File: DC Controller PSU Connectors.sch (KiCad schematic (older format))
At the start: 9 parts, among them J1 SM08B-CPTK-1A-TBL, J10 Conn_01x04, J17 Conn_01x04, J2 Conn_02x20_Odd_Even, J3 SM02B-CPTK-1A-TB, J5 BM02B-CPTK-1A-TB, J6 BM50B-SHLDS-G-TFT, J7 SM08B-CPTK-1A-TB, J8 BM08B-CPTK-1A-TB

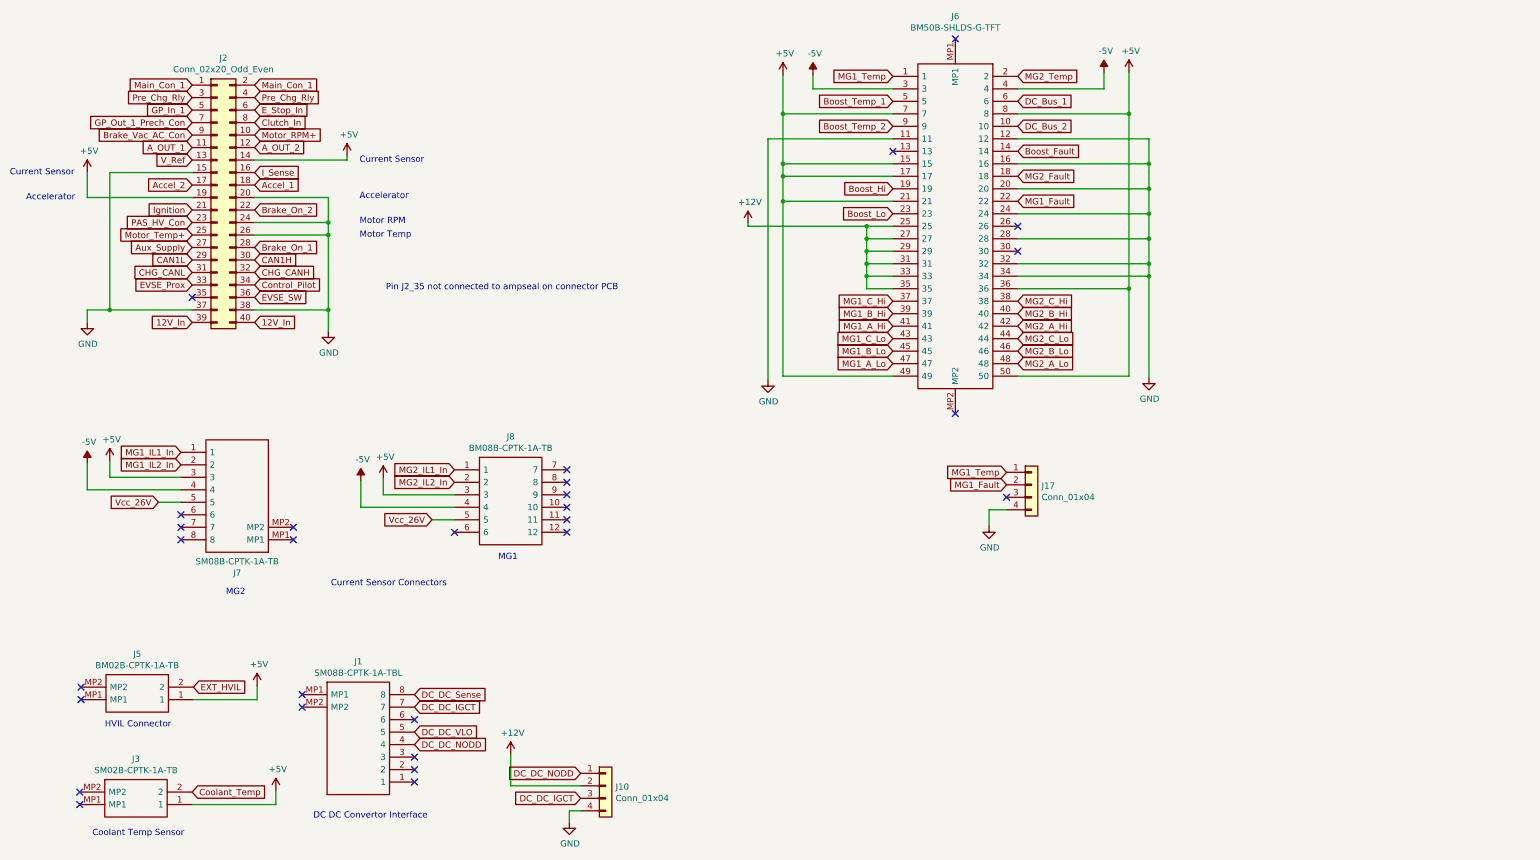
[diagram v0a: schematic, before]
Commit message: removed SG3204 and TX4313 -5V charge pumps and added LM2776 in their place
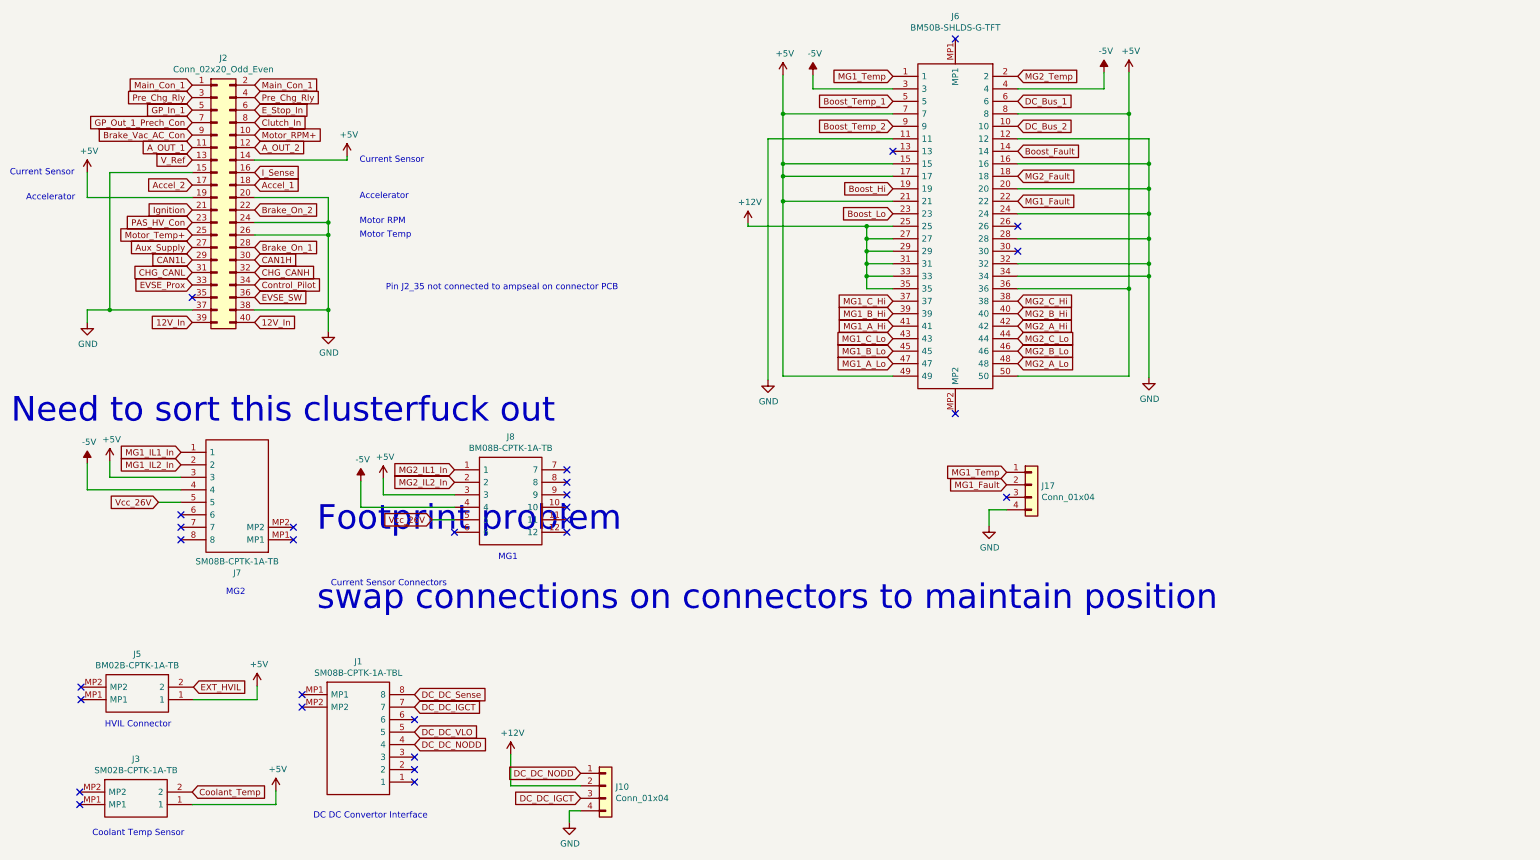
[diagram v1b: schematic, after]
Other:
- note added: "Footprint problem\n\nswap connections on connectors to maintain position"
- note added: "Need to sort this clusterfuck out"
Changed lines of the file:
@@
 	1    0    0    -1
 $EndComp
+Text Notes 800  3950 0    197  ~ 0
+Need to sort this clusterfuck out
+Text Notes 3250 5450 0    197  ~ 0
+Footprint problem\n\nswap connections on connectors to maintain position
 $EndSCHEMATC
